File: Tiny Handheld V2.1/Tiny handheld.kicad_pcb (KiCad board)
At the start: 2 copper layers, 34.3 x 58.4 mm, 44 parts, among them IC1 BQ21040DBVR, J1 VDisplay/prog1, J2 HDisplay/prog, J3 USB_C_Receptacle_USB2.0, U1 ATtiny85-20P, U2 ATtiny85-20S

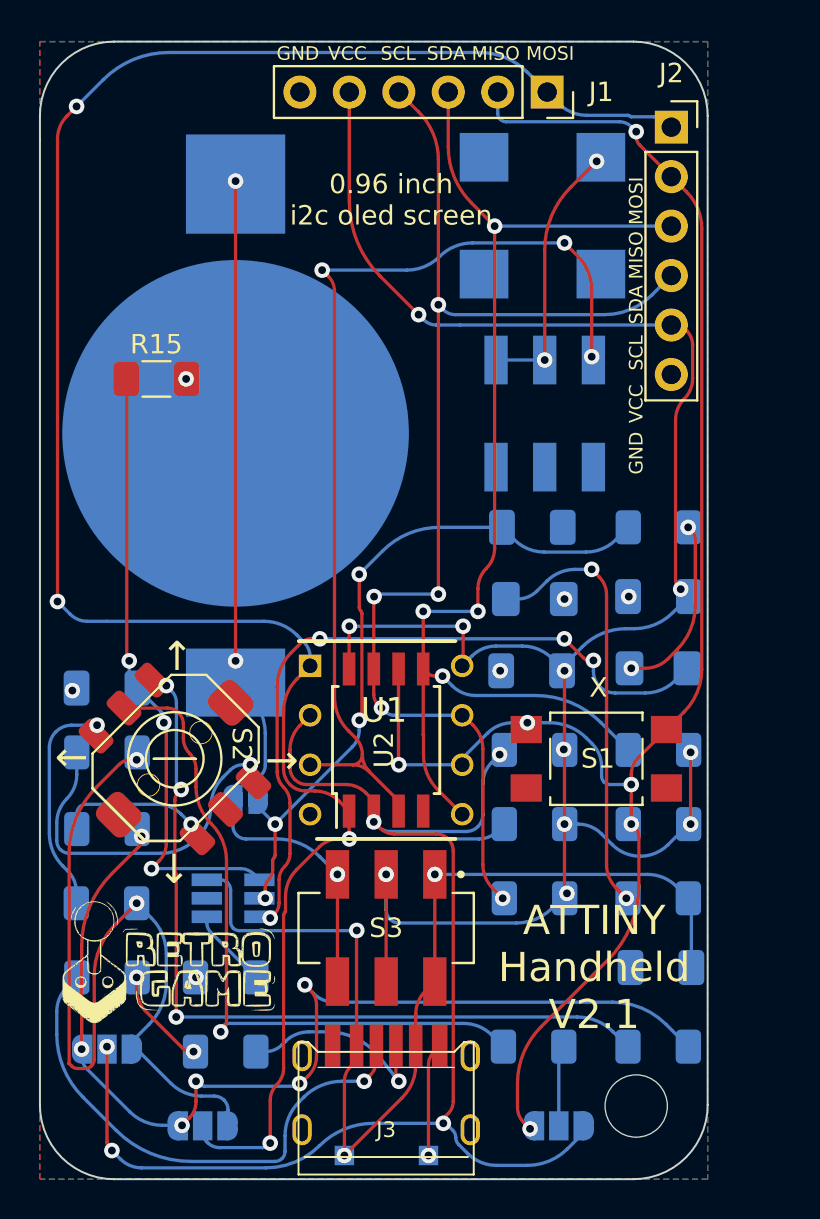
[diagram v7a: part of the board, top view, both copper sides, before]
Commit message: Fixed Silkscreen error
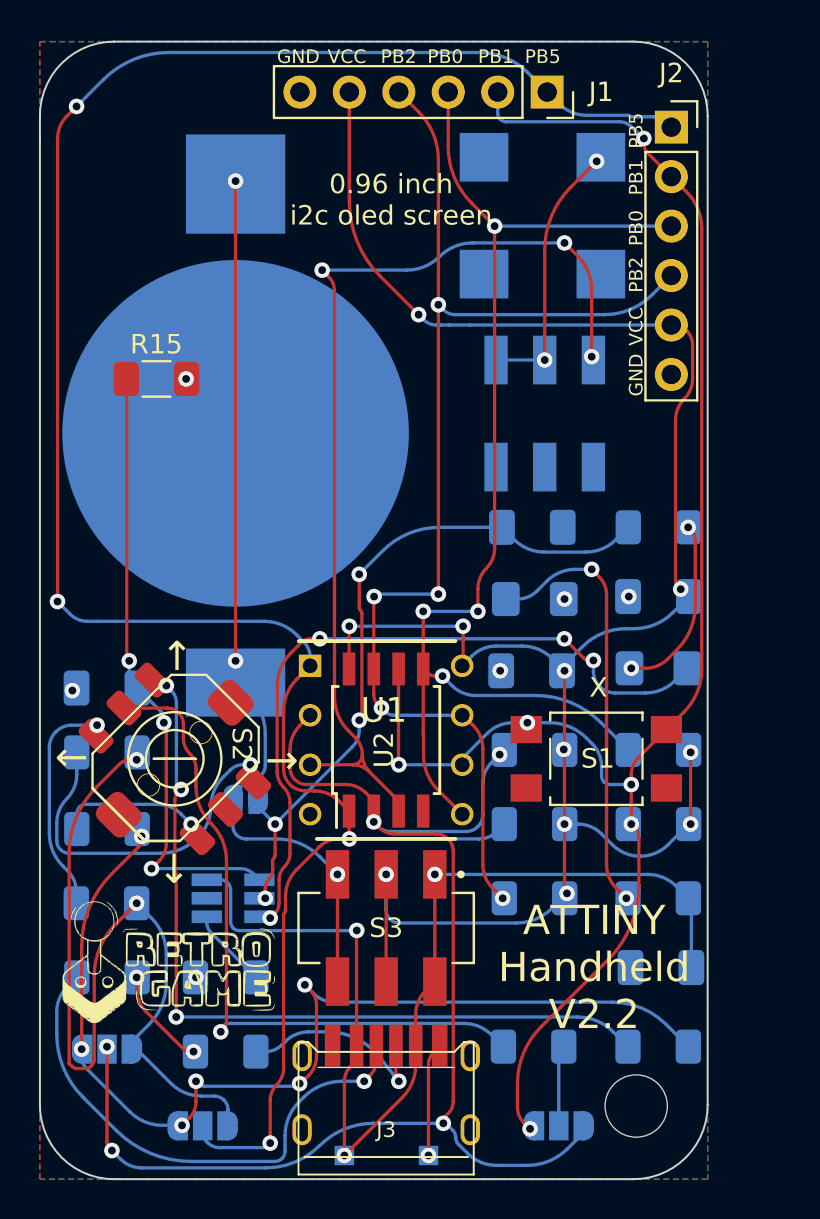
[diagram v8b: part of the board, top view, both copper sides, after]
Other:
- board text added: "ATTINY Handheld V2.2"
- board text added: "PB0"
- board text added: "PB1"
- board text added: "PB2"
- board text added: "PB5"
- board text removed: "ATTINY Handheld V2.1"
- board text removed: "MISO"
- board text removed: "MOSI"
- board text removed: "SCL"
- board text removed: "SDA"
